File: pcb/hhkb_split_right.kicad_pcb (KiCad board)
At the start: 4 copper layers, 173.7 x 97.4 mm, 83 parts, among them SW1 6, SW10 Y, SW11 U, SW12 I, SW13 O, SW14 P, SW15 [, SW16 ], SW17 Del, SW18 H, SW19 J, SW2 7, SW20 K, SW21 L, SW22 ;, SW23 ', SW24 Enter, SW25 N, SW26 M, SW27 ,, SW28 ., SW29 /, SW3 8, SW30 Shift, SW31 Fn, SW32 R-Space, SW33 Meta, SW34 Alt, SW4 9, SW5 0, SW6 -, SW7 =, SW8 \, SW9 `, U1 74HC595, U2 74HC595

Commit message: 本体基板の配線が通った（3 基板すべて DRC 違反 0・未配線 0）
Freerouting が詰まっていた原因は 3 つあり、すべて実験で特定した。

1. J_DB（FFC）がダイオード列に載っていた。上段キーのダイオードは帯へ
   1.75mm 食い込み 19.05mm ピッチで並ぶ。帯の部品で J_DB だけ背が高く
   （7.9mm）、その x がちょうど D3 の列だった。短絡・コートヤード重なり・
   ROW0 の未配線はすべてこれが原因。J_DB とその玉突きで C_BULK / C_MCU を
   ダイオードの隙間へ移した

2. GND パッドがベタに届かなかった。GND ベタは In1.Cu の 1 層だけ、GND
   パッドは全部 B.Cu の SMD。間のビアを Freerouting 任せにすると、混んだ
   区画でファンアウトに失敗する（対応 SMD ピンの 42% しか成功しなかった）。
   tools/gnd_fanout.py で配置段階に決定的に立てる

3. ピンが空の (net GND) を DSN に残すと Freerouting が NPE で落ちる。
   GND はネット定義・クラス・plane をまとめて消す。ファンアウトの配線材は
   (type protect) にしてネット無しの固定障害物として渡す（消すと避けない）

ImportSpecctraSES は既存配線を作り直すのでファンアウトが消える
（実測 7 個 → 0 個）。取り込み後に立て直している。

WIP_BOARDS が空になった。DRC の検査が skip ではなく PASS で通る。
検査 249 件通過、組み立て干渉 0。

Co-Authored-By: Claude Opus 5 <noreply@anthropic.com>
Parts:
- moved J_DB 8.50 mm to (126.5, 68.2)
- moved C_BULK 5.00 mm to (137.0, 69.1)
- moved C_MCU 5.00 mm to (145.0, 69.1)
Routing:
- net ROW4: track 230.1 -> 148.8 mm
- net ROW3: track 271.7 -> 191.7 mm
- net V3V3: track 121.2 -> 73.1 mm, vias 8 -> 0
- net ROW2: track 197.8 -> 166.5 mm
- net COL2: track 114.0 -> 90.9 mm, vias 4 -> 3
- net COL1: track 97.7 -> 76.0 mm, vias 4 -> 2
- net COL7: track 104.8 -> 85.7 mm
- net COL3: track 88.2 -> 75.0 mm
- net VBATT_SW: track 36.0 -> 24.1 mm, vias 2 -> 0
- net COL5: track 113.8 -> 102.7 mm
- net VBATT_SENSE: track 40.1 -> 29.4 mm, vias 4 -> 0
- net COL6: track 57.8 -> 47.5 mm
- net VBATT_RAW: track 27.8 -> 17.9 mm
- net COL8: track 81.5 -> 72.4 mm
- net COL4: track 109.0 -> 100.3 mm
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
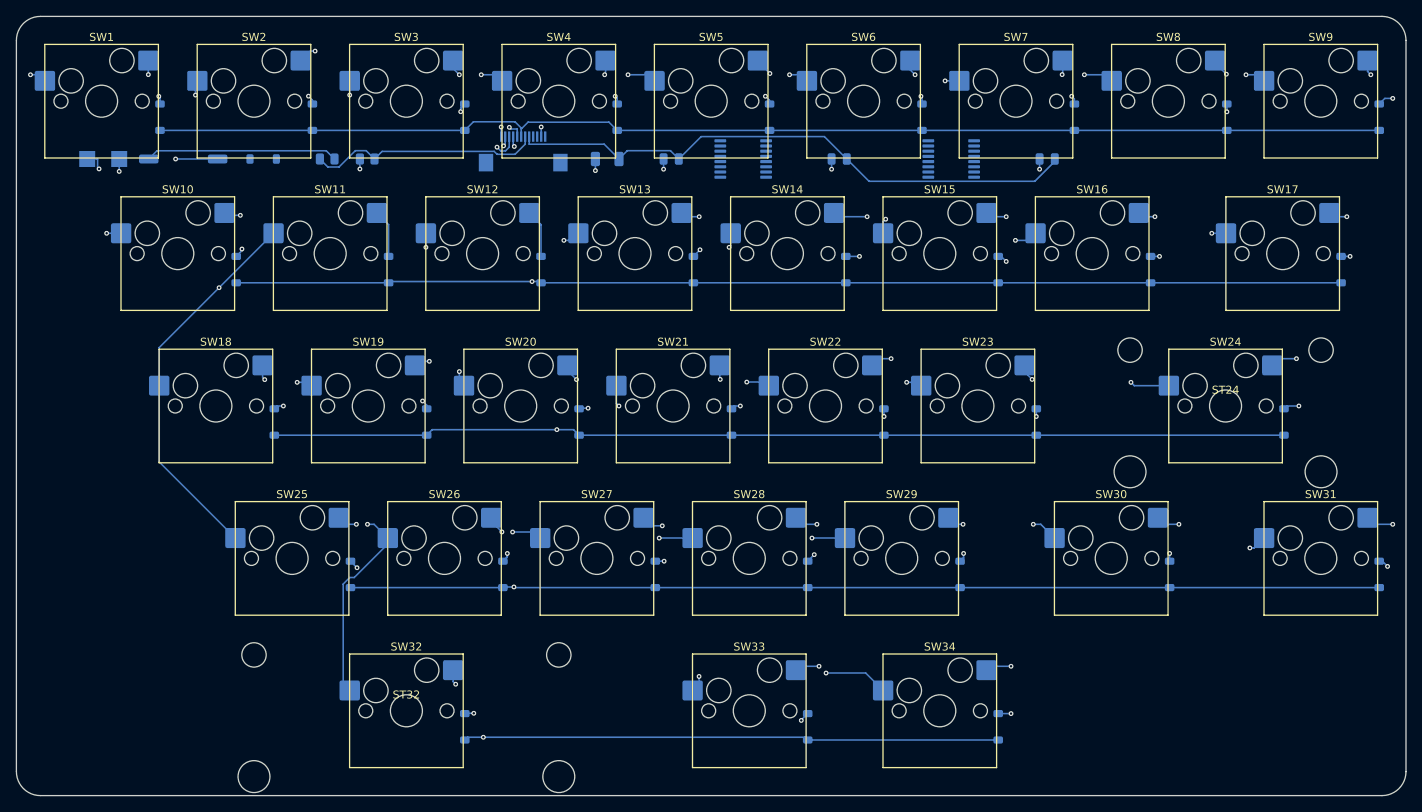
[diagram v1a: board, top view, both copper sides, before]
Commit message: 手書きルータを削除し、GND 面とファンアウトの検査を足した
gen_pcb.py は配置・ネット・ゾーン・設計規則だけになった（812→501 行）。
_route / _route_electronics / _link / _clear_x / _fcu_verticals /
_nearest_via / _track / _via / _pad / _npth_holes と、レーン関係の定数を削除。

検査を 2 つ追加。どちらも故意に壊して落ちることを確認済み。

- In1.Cu に配線が無いこと（GND 基準面が切られていない）。
  _protect_the_ground_plane を外すと左 38 本・右 65 本が In1 に引かれる。
  **DRC はこれを何も言わない。**分割の 2.4GHz にとって基準面の連続性は
  4 層にした理由そのものなので、ここは機械で守る
- 電子部品の GND パッドの脇にビアがあること。SES 取り込み後の
  再ファンアウトを外すと未配線が左 6・右 7 件出る

配線の質（手書き → Freerouting）:
  総長  左 1817→1574mm / 右 2290→1940mm
  ビア  左 58→68 / 右 68→111
  遠回りの最大  2.3→1.6
  In1.Cu の配線 0 本・GND の島 1 個 は据え置き
  DRC 違反 左 33→0 / 右 32→0

F.Cu は 0 本。信号は In2.Cu と B.Cu で足りている。

Co-Authored-By: Claude Opus 5 <noreply@anthropic.com>
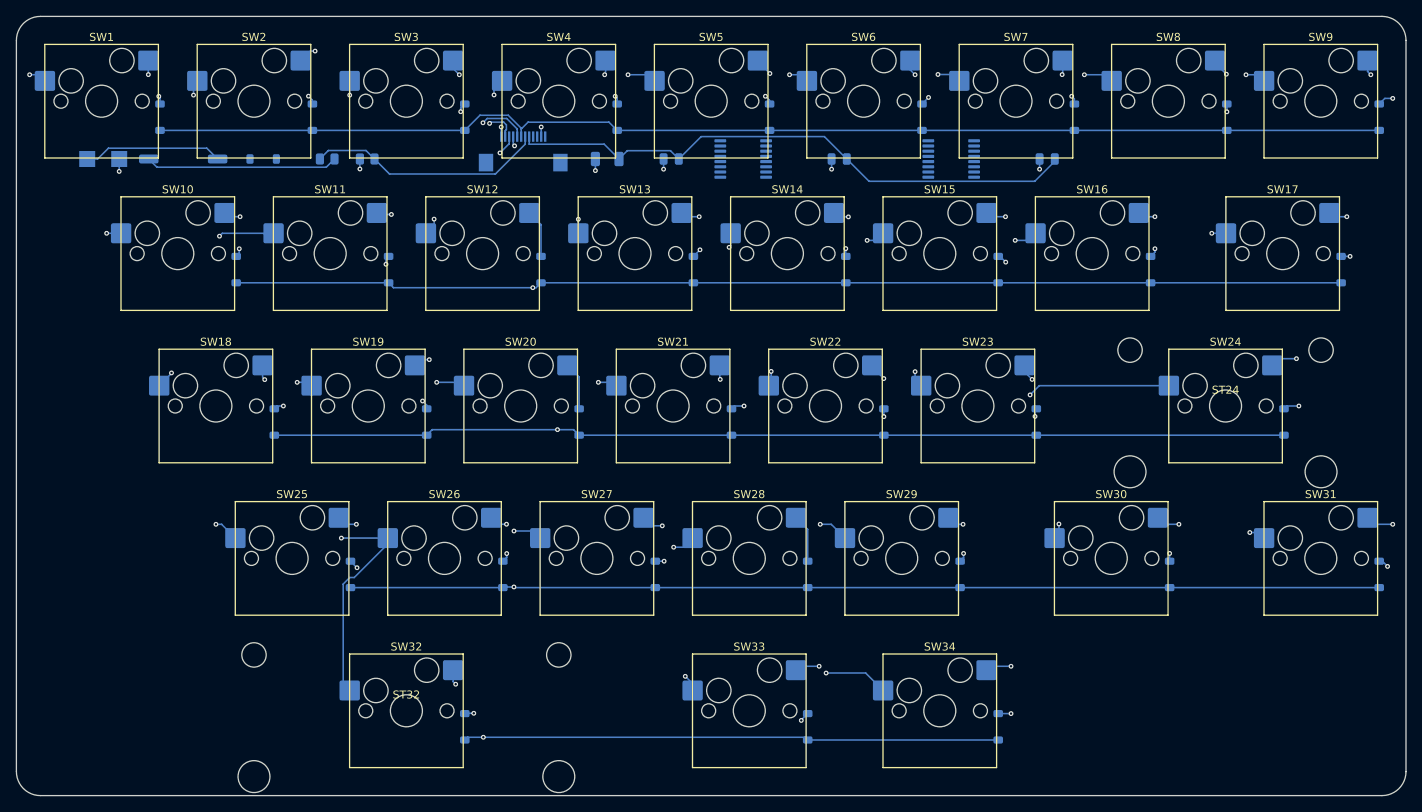
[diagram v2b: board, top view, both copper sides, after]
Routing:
- net ROW1: track 161.0 -> 168.0 mm
- net ROW4: track 148.8 -> 155.0 mm
- net SW14_D: track 11.4 -> 7.06 mm
- net COL4: track 100.3 -> 96.1 mm
- net SW11_D: track 6.03 -> 9.51 mm, vias 0 -> 2
- net SW22_D: track 11.3 -> 8.00 mm
- net COL2: track 90.9 -> 94.1 mm
- net COL6: track 47.5 -> 50.7 mm
- net COL7: track 85.7 -> 88.5 mm
- net COL8: track 72.4 -> 70.3 mm
- net SW28_D: track 8.04 -> 6.03 mm, vias 2 -> 0
- net COL5: track 102.7 -> 101.0 mm
- net SW20_D: track 7.58 -> 6.03 mm, vias 2 -> 0
- net ROW3: track 191.7 -> 190.5 mm
- net COL3: track 75.0 -> 73.8 mm
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
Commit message: スイッチ→ダイオードを自分で引き、ビアを 4〜5 割減らした
自動配線器が数 mm の接続のために内層へ往復し、SW*_D だけで左 30 個・
右 62 個のビアを使っていた（右が多いのは列のバスが 9 本あって裏面が
混むため）。ソケットの端子とダイオードのアノードは同じ x に並べてあり
（DIODE_OFFSET はそのために選んだ値）、裏面の L 字 2 本で届く。
**経路に選択の余地が無い**ので prewire_switch_diode で自分で引き、
GND と同じく DSN からネットごと外して (type protect) で渡す。

  ビア 左 68→40 / 右 111→51   総長 左 1574→1538 / 右 1940→1902mm
  左右の比 1.28 がキー数の比 1.26 とほぼ一致し、非対称が規模差だけで
  説明できるようになった。DRC は 0/0 のまま

FFC が子基板まで届くかの検査を足した。J_DB を左 9.1mm・右 8.5mm
動かしたのに、それを見る検査が無かった（ケーブルは発注品なので、
合わないと分かるのが組み立て時になる）。左 92.1mm / 右 78.5mm 要り、
100mm で足りる。FFC_LENGTH / FFC_SLACK は暫定値として登録。
左右で同じケーブルが使えることも見る（部品表を 2 種類にしない）。

検査を書く途中で test_pcb.footprints() が信用できないと分かった。
`.*?` で最初の (at ...) を拾うため、J_DB では左が誤った座標・右が空を
返す。この検査では括弧の対応で切り出す _footprint_blocks を使った。

Co-Authored-By: Claude Opus 5 <noreply@anthropic.com>
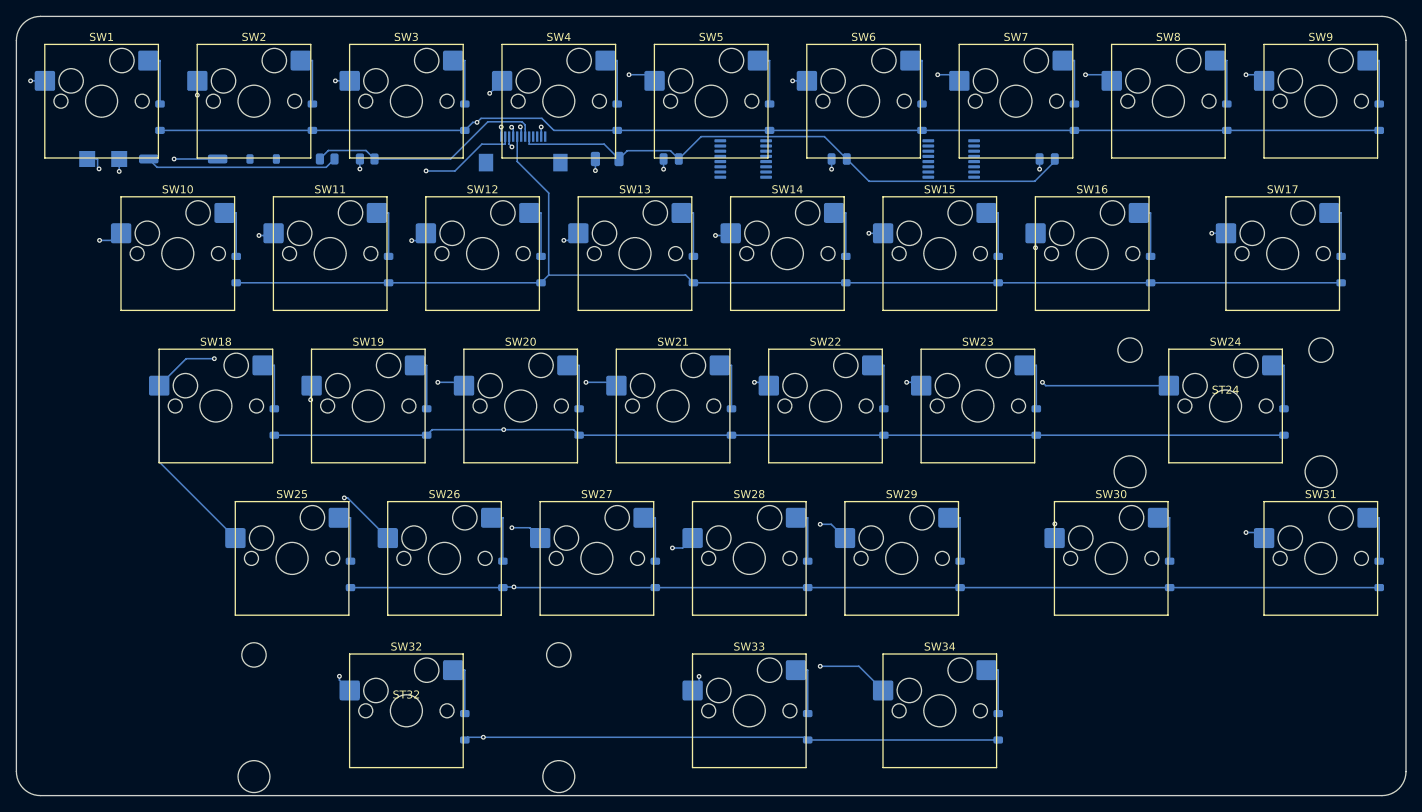
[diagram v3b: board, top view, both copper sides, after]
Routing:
- net ROW1: track 168.0 -> 157.9 mm, vias 2 -> 0
- net ROW2: track 167.0 -> 172.8 mm
- net COL7: track 88.5 -> 82.9 mm
- net SW33_D: track 12.0 -> 6.89 mm, vias 2 -> 0
- net ROW0: track 155.7 -> 160.6 mm, vias 0 -> 2
- net SW24_D: track 11.4 -> 6.89 mm, vias 2 -> 0
- net COL4: track 96.1 -> 100.5 mm
- net SW34_D: track 10.8 -> 6.89 mm, vias 2 -> 0
- net SW31_D: track 10.3 -> 6.89 mm, vias 2 -> 0
- net SW11_D: track 9.51 -> 6.89 mm, vias 2 -> 0
- net SW15_D: track 9.49 -> 6.89 mm, vias 2 -> 0
- net COL8: track 70.3 -> 67.7 mm
- net SW2_D: track 9.45 -> 6.89 mm, vias 2 -> 0
- net SW25_D: track 9.15 -> 6.89 mm, vias 2 -> 0
- net COL3: track 73.8 -> 75.8 mm
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
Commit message: 電源スイッチを基板から外し、背面パネルへ（open-gaps #17 解決）
基板の後端からケース背面まで 23.3mm あり、基板の上のどこに置いても
背面には出せない。「基板に載せる」という前提自体が誤りだった。

SW_PWR の種類を wire_pads にし、基板は SW_PWR_1 / SW_PWR_2 の
ランド 2 個で受ける。電池ボックスと同じ形。実物は背面パネルに付けて
配線で繋ぐ。部品はプッシュロック（オルタネート）の丸ボタン
（実機の「電源／Bluetooth ペアリング」も丸ボタン。機械接点なので
電池を本当に切り離せる）。

再発防止に test_no_user_operated_part_is_sealed_inside を追加。
故意にスイッチを基板へ戻すと落ちることを確認済み。**最初に書いた版は
空振りしていた**（配線済み基板を読むのに再生成しか走らせておらず、
検査対象が変わっていなかった）。配線まで通して確かめ直した。

ランド 2 個への展開規則を circuit.board_refs に一本化した。
gen_pcb と test_pcb と test_conformance が別々に「battery_holder だけ
2 個」と持っていたため、電源スイッチを変えた瞬間に検査 6 件が落ちた。

検査 260 件通過。DRC は 3 基板とも 0/0 のまま。

Co-Authored-By: Claude Opus 5 <noreply@anthropic.com>
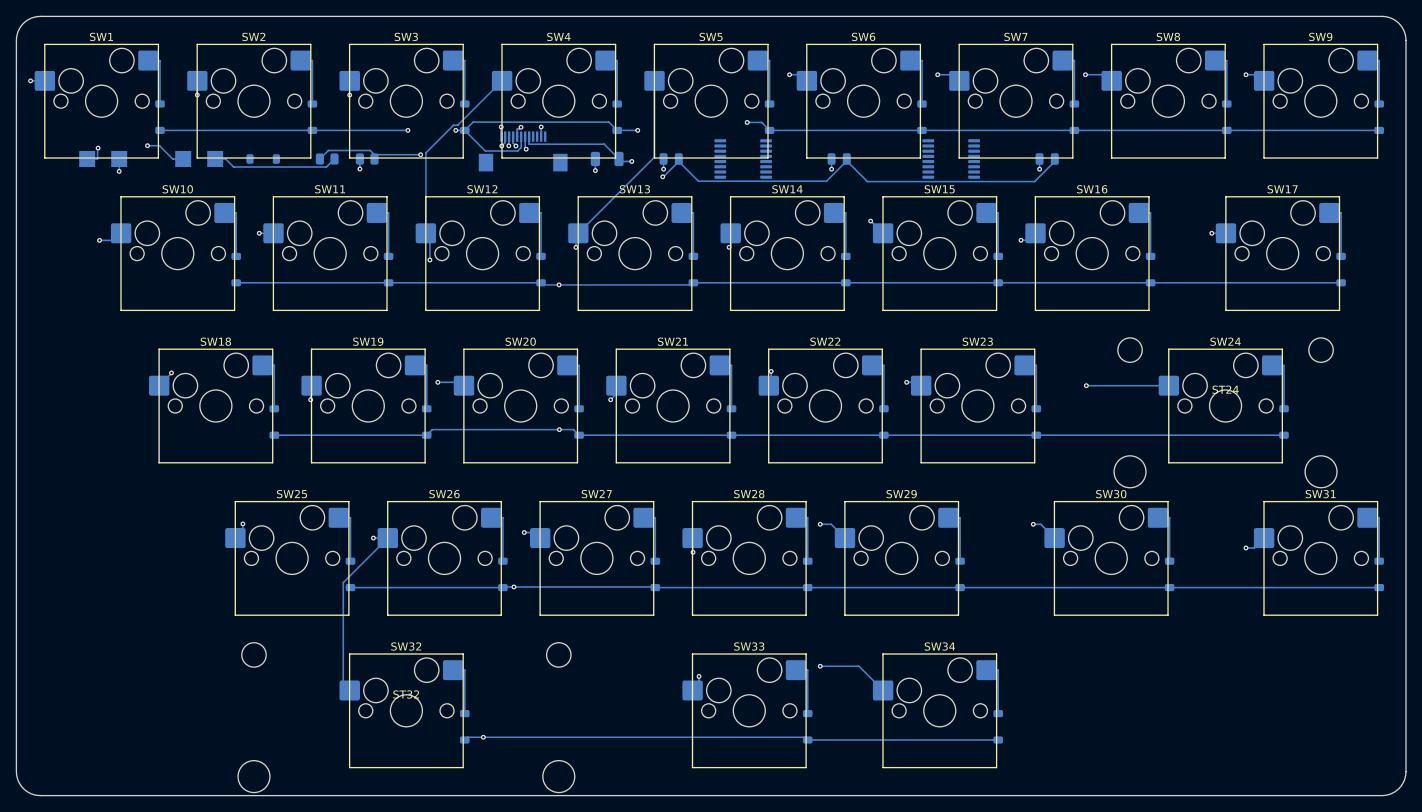
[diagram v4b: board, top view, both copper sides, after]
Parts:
- removed SW_PWR: slide_switch, SW_DIP_SPSTx01_Slide_9.78x4.72mm_W8.61mm_P2.54mm
- added SW_PWR_1: wire_pads, TestPoint_Pad_2.0x2.0mm, B.Cu at (84.0, 69.1)
- added SW_PWR_2: wire_pads, TestPoint_Pad_2.0x2.0mm, B.Cu at (88.0, 69.1)
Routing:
- net COL4: track 100.5 -> 90.8 mm, vias 5 -> 4
- net VBATT_SW: track 24.1 -> 15.7 mm
- net ROW4: track 155.8 -> 149.0 mm
- net ROW2: track 172.8 -> 167.4 mm
- net COL2: track 94.5 -> 89.6 mm, vias 4 -> 3
- net COL3: track 75.8 -> 71.5 mm, vias 4 -> 3
- net VBATT_RAW: track 17.9 -> 14.1 mm
- net ROW1: track 157.9 -> 161.5 mm, vias 0 -> 2
- net ROW0: track 160.6 -> 163.8 mm, vias 2 -> 4
- net COL7: track 82.9 -> 85.5 mm
- net COL8: track 67.7 -> 69.8 mm
- net V3V3: track 73.1 -> 74.2 mm, vias 0 -> 2
- net COL1: track 73.7 -> 74.2 mm, vias 3 -> 4
- net VBATT_SENSE: track 30.1 -> 29.8 mm, vias 0 -> 2

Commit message: 電源スイッチの決定を記録し、追随できていなかった 3 箇所を直した
decisions/2026-08-08-power-switch.md を追加。基板に載せない理由
（後端から背面まで 23.3mm）、丸ボタンでなくスライドにした理由
（左の枠が幅 10.6mm しかなく、直径がそのまま幅を食う丸型は不利）、
覆す前に読むことを残した。

**変更に追随できていなかった箇所を 3 つ見つけて直した:**

1. test_resources.py の部品表が古かった。595 が SOIC-16（7.4x10.4）の
   ままで、基板から外した「スライドスイッチ 9.0x5.0」も残っていた。
   TSSOP-16（7.79x5.59）と「電源スイッチのランド 4.0x4.0 x2」へ。
   この表は「書き漏らすと誰も気づかない」ためのものなので、古いままだと
   目的を果たさない
2. gen_pcb.py の嘘コメント 2 つ（「手前の帯に電源。手が届く側に置く」
   「スライドスイッチは 9.78x4.72mm。帯に収まる」）
3. gnd_fanout.py の ELEC 正規表現が SW_PWR 止まりで SW_PWR_1 を拾えない

3 は test_pcb.py の ELEC_REF と同じ式の二重管理だった。circuit.py へ
一本化した（board_refs / WIRE_PAD_KINDS と同じ理由）。

実機との差を open-gaps #20 に記録（形式・機能・位置）。

検査 262 件通過。DRC は 3 基板とも 0/0。

Co-Authored-By: Claude Opus 5 <noreply@anthropic.com>
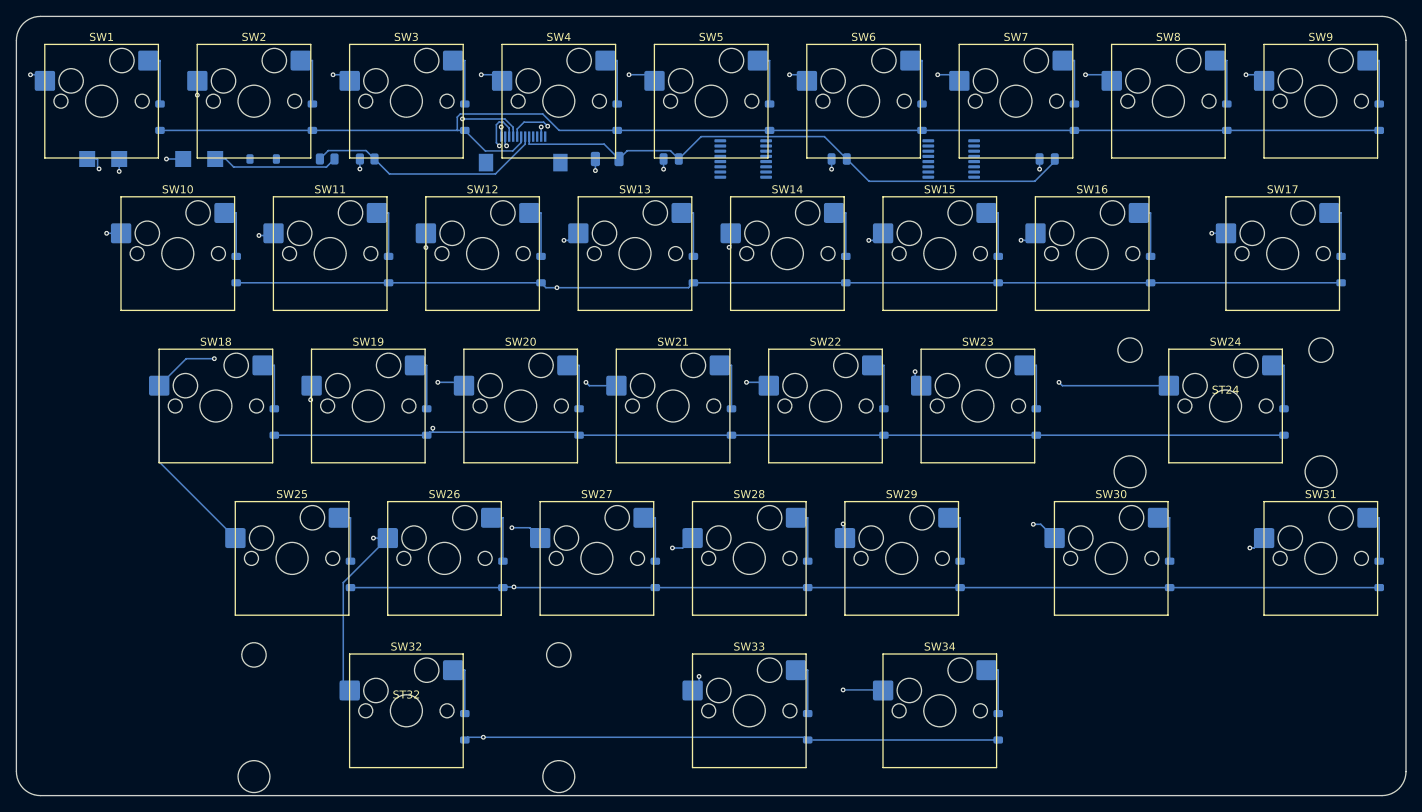
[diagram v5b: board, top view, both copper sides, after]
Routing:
- net COL4: track 90.8 -> 100.3 mm, vias 4 -> 5
- net ROW2: track 167.4 -> 176.4 mm
- net COL3: track 71.5 -> 76.2 mm, vias 3 -> 4
- net ROW3: track 190.2 -> 194.4 mm
- net COL2: track 89.6 -> 93.6 mm
- net ROW1: track 161.5 -> 164.6 mm
- net COL8: track 69.8 -> 72.4 mm
- net ROW0: track 163.8 -> 165.3 mm, vias 4 -> 0
- net V3V3: track 74.2 -> 73.1 mm, vias 2 -> 0
- net COL5: track 101.0 -> 100.1 mm
- net COL0: track 28.4 -> 27.7 mm
- net COL6: track 51.0 -> 50.3 mm
- net COL1: track 74.2 -> 73.7 mm, vias 4 -> 3
- net VBATT_SENSE: vias 2 -> 0

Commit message: 1 回発注に合わせ、アンテナで無料でできることを全部やった
発注を 1 回にまとめると決めたので、**発注前に測る手段が無くなった。**
そこで方針を「測るまで止める」から「無料の対策を全部やる＋手戻りを
子基板 1 枚に閉じ込める」へ変えた。

**新たに 3 つの案を数字で潰した**（open-gaps #23 の表に追記）:
- 子基板の銅を抜く … アンテナの影 3mm のうち 2mm が FFC コネクタの下
- 90° 回す（再検討）… 左はアンテナと電池が -0.6mm（必要 10mm）
- 右の子基板を空いた x へ … どこに置いても最良で 9 本掛かる

**やったこと: 本体基板の禁止域（左のみ）。**
一度「支配的でない」として捨てた案を入れ直した。無料だから。
左は 30x15mm を全層で禁止域にでき、配線を 1 本も動かさずに入った
（DRC 0 のまま。ビア +1・配線 +4mm）。右は列のバス 9 本が横断していて
入らない。**Freerouting 2.3.0 は DSN の禁止域を守らない**（4 層とも
正しく出ていることは確認）。左が通ったのは偶然そこを使わなかっただけ。

効き目は限定的なはず。波長 125mm に対して窓が小さい。
**「やらないよりまし」以上の主張はしない。**

手戻りの封じ込め:
- test_the_cable_interface_is_frozen が FFC の界面を凍結。子基板を
  作り直しても本体基板 2 枚とケーブルは無傷
- 止め具を「承知の記録が無いまま製造ファイルを出すな」へ書き換えた
  （子基板だけ先に出す前提が消えたため）

**設定しただけでは効いていない**ので 2 つ検査を足した:
- test_the_antenna_keepout_is_actually_empty（実基板に銅が無いこと）
- test_the_antenna_keepout_covers_the_real_antenna（ケース側と位置照合）
どちらも故意にずらして落ちることを確認した。

autoroute.py の java 選びも直した。macOS の /usr/bin/java は存在するが
実行すると失敗するスタブで、存在検査だけだとこれを選んで**配線が黙って
失敗する**（実際に起きた）。-version が通ることまで見る。

3 基板とも DRC 0 / 未配線 0。組み立て干渉 0。検査 282 件。

Co-Authored-By: Claude Opus 5 (1M context) <noreply@anthropic.com>
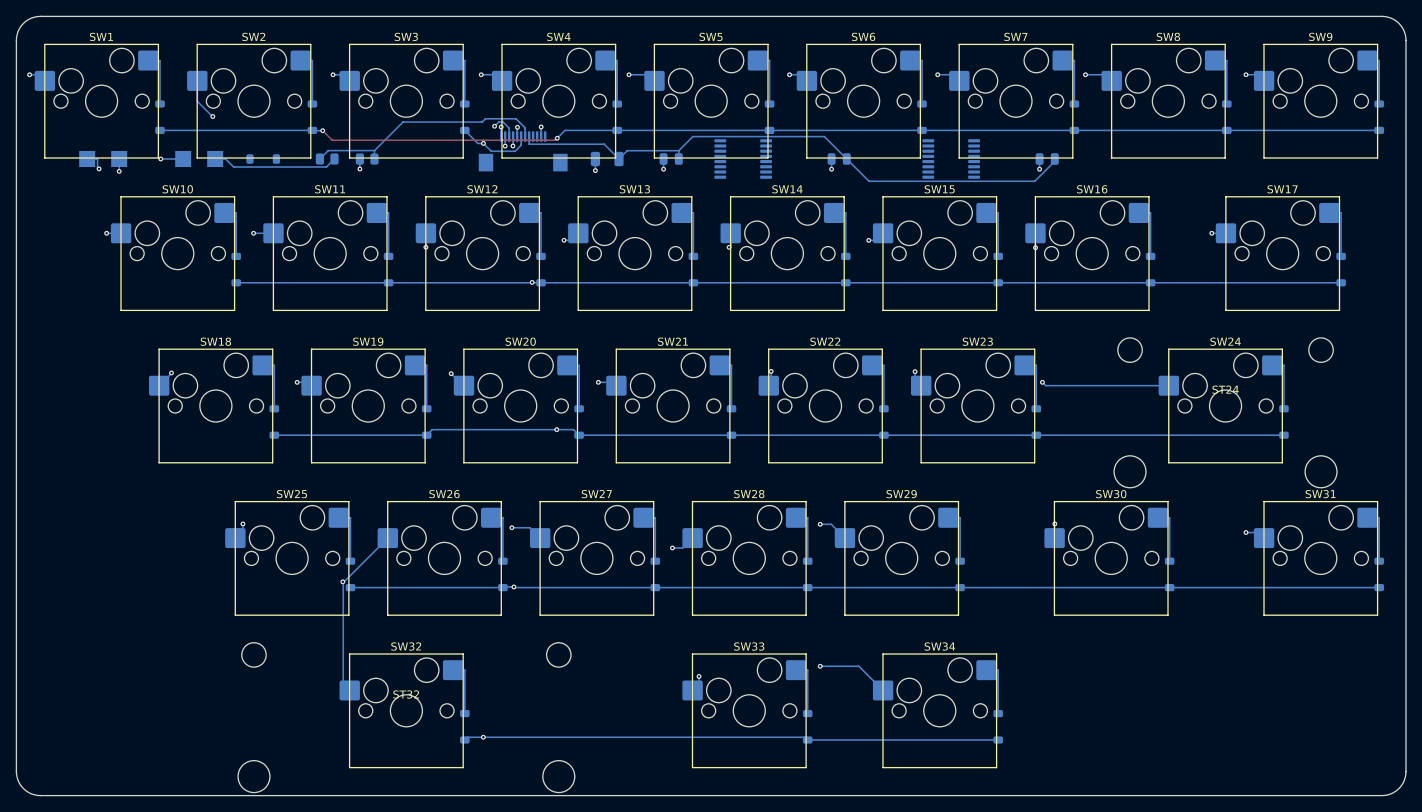
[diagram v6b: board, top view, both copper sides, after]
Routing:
- net ROW2: track 176.4 -> 167.3 mm
- net COL2: track 93.6 -> 99.1 mm
- net COL8: track 72.4 -> 67.7 mm
- net ROW1: track 164.6 -> 160.1 mm
- net COL7: track 85.9 -> 82.9 mm
- net ROW0: track 165.3 -> 163.3 mm, vias 0 -> 3
- net COL4: track 100.3 -> 98.8 mm
- net COL3: track 76.2 -> 74.9 mm
- net COL1: track 73.7 -> 74.8 mm, vias 3 -> 4
- net COL5: track 100.1 -> 101.0 mm
- net VBATT_SENSE: track 29.8 -> 30.3 mm
